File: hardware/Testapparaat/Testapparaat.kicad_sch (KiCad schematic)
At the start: 6 parts

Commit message: -enh Made the schematic for the main unit almost complete :)
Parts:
- added J7: Emergency Stop Button, symbol Connector:Mini-DIN-3
- added R14, R15, R16, R17, R18, R19, R? (x2): 10k, symbol Device:R
- added R20: 1k, symbol Device:R
- added SW3: Menu, symbol Switch:SW_Push
- added SW4: Go Back, symbol Switch:SW_Push
- added SW5: RotaryEncoder_Switch, symbol Device:RotaryEncoder_Switch
- added SW6: START, symbol Switch:SW_Push
- added SW7: STOP, symbol Switch:SW_Push
- added U4: 74AUC1G74, symbol 74xGxx:74AUC1G74
- added U5: TCA9534 (IO Expander), symbol Interface_Expansion:TCA9534
- U1: renamed from U?; value 74HC595 -> 74HC595 (SIPO Shift register)
- gave numbers to parts that had none: 5
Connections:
- net OE is gone; now on net GND: U1.13 (~{OE})
- net +3.3V: now also R14.1, R15.1, R16.1, R17.1, R18.1, R19.1, R20.1, SW5.C, U4.7 (~{PRE}), U4.8 (VCC), U5.16 (VDD)
- net GND: now also J7.2, R?.2, R?.2, SW3.2, SW4.2, SW5.S2, SW6.2, SW7.2, U4.4 (GND), U4.6 (~{CLR}), U5.1 (A0), U5.2 (A1), U5.3 (A2), U5.8 (GND)
- net I2C_SCL: now also U5.14 (SCL)
- net I2C_SDA: now also U5.15 (SDA)
- net STATUS_MOD_1: now also U1.5 (QF); no longer U1.7 (QH)
- net STATUS_MOD_2: now also U1.4 (QE); no longer U1.6 (QG)
- net TTL1_MOD_2: now also U1.2 (QC); no longer U1.3 (QD)
- net TTL2_MOD_2: now also U1.3 (QD); no longer U1.4 (QE)
- net TTL3_MOD_1: now also U5.4 (P0); no longer U1.2 (QC)
- net TTL3_MOD_2: now also U5.5 (P1); no longer U1.5 (QF)
- net SRCLR: no longer names the net of U1.10 (~{SRCLR})
- net SRCLR: now also R20.2
- new net BACK_BTN: R15.2, SW4.1, U5.10 (P5)
- new net Display_DC: U1.7 (QH)
- new net Display_RST: U1.6 (QG)
- new net EMERGENCY_STOP_BTN: J7.3, R19.2
- new net ENCODER_BTN: R16.2, SW5.S1, U5.11 (P6)
- new net IO_EXP_INT: U5.13 (~{INT})
- new net MENU_BTN: R14.2, SW3.1, U5.9 (P4)
- new net Rotary_B: R?.1, SW5.B, U4.2 (D)
- new net Rotary_CLK: R?.1, SW5.A, U4.1 (C)
- new net Rotary_DT: U4.5 (Q)
- new net START_BTN: R18.2, SW6.1, U5.6 (P2)
- new net STOP_BTN: R17.2, SW7.1, U5.7 (P3)
- no-connect marks 26 -> 28
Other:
- sheet Power Supply ports: added 5V_OUT, BATT_OUT+, BATT_OUT-; removed none
- note added: "Emergency stop using hardware (logic) is better"
- note added: "GPIO Expanders / Shift registers"
- note added: "MCU, Display, IO, SD"
- note added: "Module Ports"
- note added: "Power Supply"
- note removed: "MCU & Display"
- moved on the sheet: J2, J3, U1

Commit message: -enh Noodstop is now hardware controlled
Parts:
- added Q? (x3): IRF540N, Package_TO_SOT_THT:TO-220-3_Vertical, symbol Transistor_FET:IRF540N
- added R?: 1k, symbol Device:R
- added U? (x2): 74HC14, symbol 74xx:74HC14
- gave numbers to parts that had none: 2
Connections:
- net +3.3V: now also Q?.2 (D), U?.14 (VCC); no longer J2.5 (Pin_5), J3.5 (Pin_5)
- net +5V: now also Q?.2 (D); no longer J2.8 (Pin_8), J3.8 (Pin_8)
- net +BATT: now also Q?.2 (D); no longer J2.4 (Pin_4), J3.4 (Pin_4)
- net EMERGENCY_STOP_BTN: now also U?.1
- net GND: now also R?.2, U?.7 (GND)
- net MOD_PSU_EN: now reaches U5.12 (P7)
- net MOD_PSU_EN: now also Q?.1 (G), Q?.1 (G), Q?.1 (G), R?.1, U?.2
- new net +3.3VP: J2.5 (Pin_5), J3.5 (Pin_5), Q?.3 (S)
- new net +5VP: J2.8 (Pin_8), J3.8 (Pin_8), Q?.3 (S)
- new net +VSW: J2.4 (Pin_4), J3.4 (Pin_4), Q?.3 (S)
- no-connect marks 28 -> 27

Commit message: -enh made some changes to schematic and assigned fp
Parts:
- removed Q? (x3): IRF540N, Package_TO_SOT_THT:TO-220-3_Vertical, symbol Transistor_FET:IRF540N
- removed R?: 1k, symbol Device:R
- added C14, C15, C16, C17, C18, C19, C20: 1u, Capacitor_SMD:C_0603_1608Metric_Pad1.08x0.95mm_HandSolder, symbol Device:C
- added D1, D2, D3, D4, D5, D6, D7: 1N4448, Diode_THT:D_DO-35_SOD27_P7.62mm_Horizontal, symbol Diode:1N4448
- added Q3: BC817, Package_TO_SOT_SMD:SOT-23, symbol Transistor_BJT:BC817
- added Q4, Q5, Q6: IRF9540N, Package_TO_SOT_THT:TO-220-3_Vertical, symbol Transistor_FET:IRF9540N
- added R23, R24, R25, R26, R27, R28, R29: 10k, Resistor_SMD:R_0603_1608Metric_Pad0.98x0.95mm_HandSolder, symbol Device:R
- added R30: 1k, Resistor_SMD:R_0603_1608Metric_Pad0.98x0.95mm_HandSolder, symbol Device:R
- added R31, R32: 100k, Resistor_SMD:R_0603_1608Metric_Pad0.98x0.95mm_HandSolder, symbol Device:R
- added unit 3 of U6
- added unit 2 of U6
- added unit 4 of U6
- added unit 6 of U6
- added unit 5 of U6
- J1: footprint (none) -> Connector_Card:microSD_HC_Hirose_DM3BT-DSF-PEJS
- J2, J3: footprint (none) -> Connector_PinHeader_2.54mm:PinHeader_2x12_P2.54mm_Horizontal
- J7: footprint (none) -> Connector_PinHeader_2.54mm:PinHeader_1x03_P2.54mm_Horizontal
- R1, R14, R15, R16, R17, R18, R19, R2, R20, R21, R22: footprint (none) -> Resistor_SMD:R_0603_1608Metric_Pad0.98x0.95mm_HandSolder
- SW3, SW6, SW7: footprint (none) -> Button_Switch_SMD:SW_SPST_B3S-1000
- SW4: value Go Back -> Back; footprint (none) -> Button_Switch_SMD:SW_SPST_B3S-1000
- SW5: footprint (none) -> Rotary_Encoder:RotaryEncoder_Alps_EC11E-Switch_Vertical_H20mm_CircularMountingHoles
- U1: footprint (none) -> Package_SO:SO-16_3.9x9.9mm_P1.27mm
- U4: footprint (none) -> Package_SO:VSSOP-8_2.3x2mm_P0.5mm
- U5: footprint (none) -> Package_SO:TSSOP-16_4.4x5mm_P0.65mm
- U6: renamed from U?; footprint (none) -> Package_SO:SO-14_3.9x8.65mm_P1.27mm
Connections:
- net +3.3V: now also R21.2, SW3.2, SW4.2, U4.6 (~{CLR}), Q4.3 (S), R26.2; no longer R14.1, R15.1, SW5.C
- net +3.3VP: now also Q4.2 (D)
- net +5V: now also Q5.3 (S)
- net +5VP: now also Q5.2 (D)
- net +BATT: now also Q6.3 (S), R31.1
- net +VSW: now also Q6.2 (D)
- net BACK_BTN: now also C15.1, D2.1 (K), R23.2; no longer R15.2, SW4.1
- net ENCODER_BTN: now also U6.12; no longer R16.2, SW5.S1
- net GND: now also R14.2, R15.2, SW5.C, C14.2, C15.2, C16.2, C17.2, C18.2, C19.2, C20.2, Q3.2 (E), R32.2; no longer R21.2, R22.2, SW3.2, SW4.2, U4.6 (~{CLR})
- net MENU_BTN: now also R22.2, C14.1, D1.1 (K); no longer R14.2, SW3.1
- net MOD_PSU_EN: now also R30.1
- net Rotary_B: now also U6.4; no longer R22.1, SW5.B
- net Rotary_CLK: now also U6.6; no longer R21.1, SW5.A
- net START_BTN: now also U6.8; no longer R18.2, SW6.1
- net STOP_BTN: now also U6.10; no longer R17.2, SW7.1
- new net: C16.1, D3.1 (K), R24.2, U6.5
- new net: D2.2 (A), R15.1, R23.1, SW4.1
- new net: C19.1, D7.1 (K), R29.2, U6.11
- new net: D4.2 (A), R25.1, R26.1, SW5.B
- new net: R21.1, SW5.A
- new net: D1.2 (A), R14.1, R22.1, SW3.1
- new net: C18.1, D6.1 (K), R28.2, U6.9
- new net: D6.2 (A), R18.2, R28.1, SW6.1
- new net: Q3.1 (B), R30.2, R32.1
- new net: C17.1, D4.1 (K), R25.2, U6.3
- new net: D7.2 (A), R17.2, R29.1, SW7.1
- new net: Q3.3 (C), Q4.1 (G), Q5.1 (G), Q6.1 (G), R31.2
- new net: D3.2 (A), R24.1
- new net: C20.1, D5.1 (K), R27.1, U6.13
- new net: D5.2 (A), R16.2, R27.2, SW5.S1
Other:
- note removed: "Emergency stop using hardware (logic) is better"
- moved on the sheet: R14, R15, R16, R17, R18, R20, R21, SW5, SW6, SW7, U1, U4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

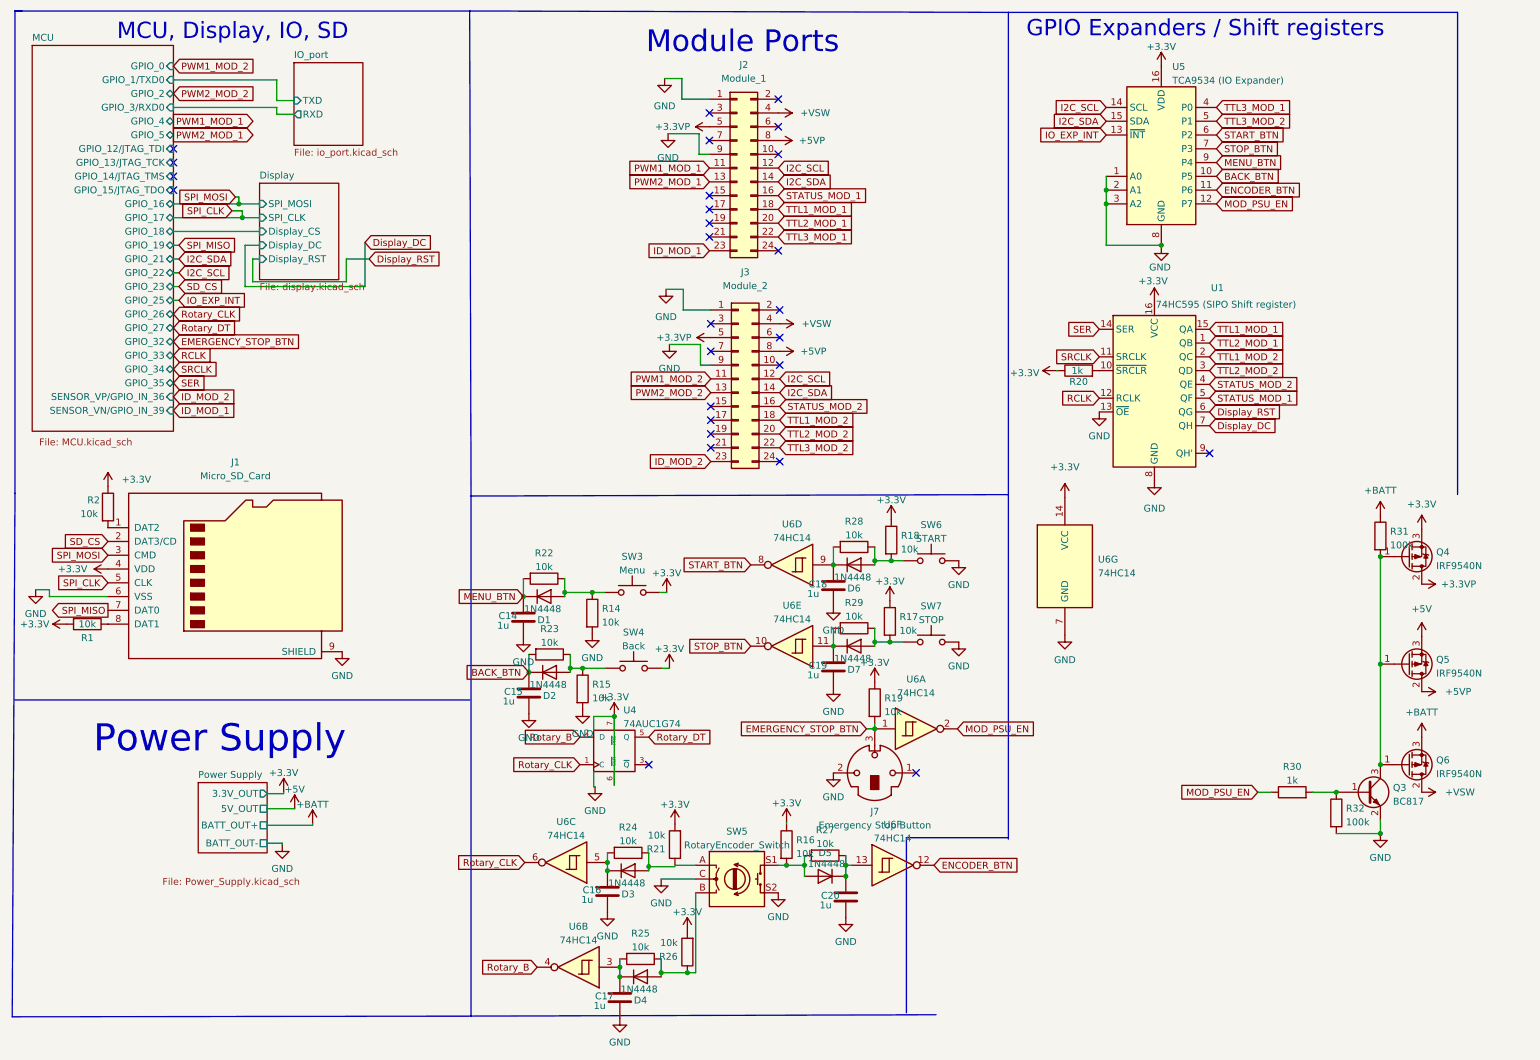
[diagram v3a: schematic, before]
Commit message: -enh add seperate schematic and pcb for io ports/slots
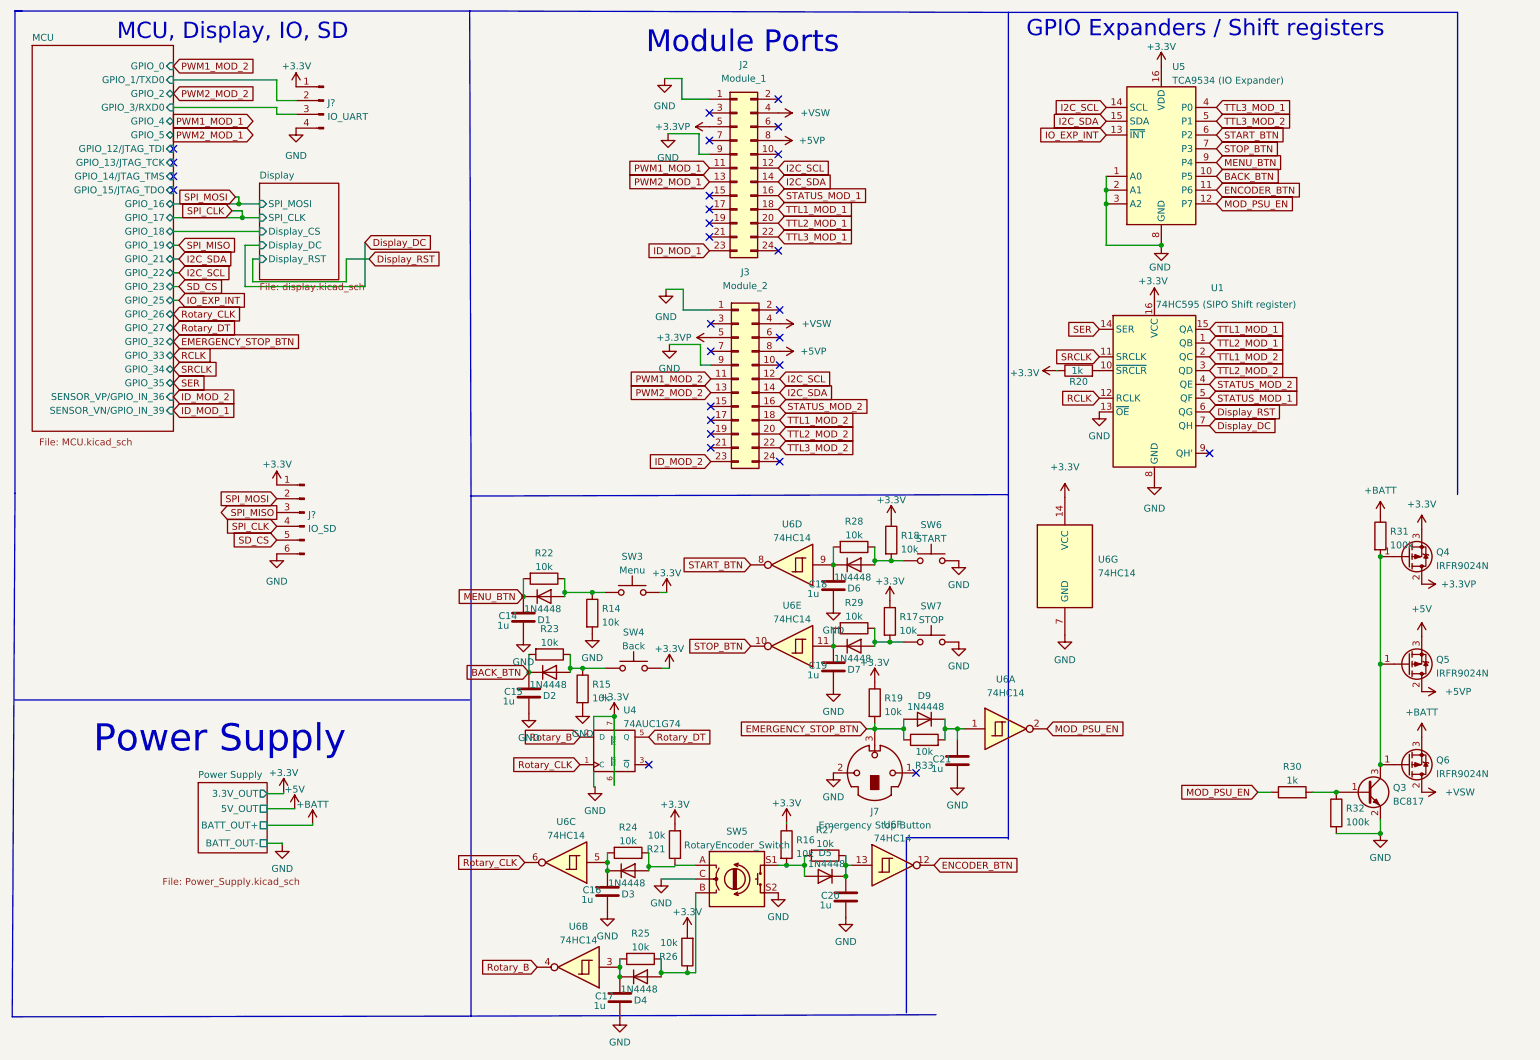
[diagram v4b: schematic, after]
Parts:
- removed J1: Micro_SD_Card, Connector_Card:microSD_HC_Hirose_DM3BT-DSF-PEJS, symbol Connector:Micro_SD_Card
- removed R1, R2: 10k, Resistor_SMD:R_0603_1608Metric_Pad0.98x0.95mm_HandSolder, symbol Device:R
- added C21: 1u, Capacitor_SMD:C_0603_1608Metric_Pad1.08x0.95mm_HandSolder, symbol Device:C
- added D9: 1N4448, Diode_THT:D_DO-35_SOD27_P7.62mm_Horizontal, symbol Diode:1N4448
- added J?: IO_UART, symbol Connector:Conn_01x04_Male
- added J?: IO_SD, symbol Connector:Conn_01x06_Male
- added R33: 10k, Resistor_SMD:R_0603_1608Metric_Pad0.98x0.95mm_HandSolder, symbol Device:R
- Q4, Q5, Q6: value IRF9540N -> IRFR9024N; footprint Package_TO_SOT_THT:TO-220-3_Vertical -> Package_TO_SOT_SMD:TO-252-3_TabPin2
- U1: footprint Package_SO:SO-16_3.9x9.9mm_P1.27mm -> 74HC595D-Q100,118:74HC595DQ100118
- U5: footprint Package_SO:TSSOP-16_4.4x5mm_P0.65mm -> TCA9534:SOP65P640X120-16N
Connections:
- net +3.3V: now also J?.1 (Pin_1), J?.1 (Pin_1)
- net EMERGENCY_STOP_BTN: now also D9.2 (A), R33.1; no longer U6.1
- net GND: now also C21.2, J?.4 (Pin_4), J?.6 (Pin_6)
- net SD_CS: now also J?.5 (Pin_5)
- net SPI_CLK: now also J?.4 (Pin_4)
- net SPI_MISO: now also J?.3 (Pin_3)
- net SPI_MOSI: now also J?.2 (Pin_2)
- new net: C21.1, D9.1 (K), R33.2, U6.1
- new net MCU/GPIO_1/TXD0: J?.2 (Pin_2)
- new net MCU/GPIO_3/RXD0: J?.3 (Pin_3)
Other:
- removed sheet IO_port
- moved on the sheet: U6A

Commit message: -add BOM
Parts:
- removed C14, C15, C16, C17, C18, C19, C20: 1u, Capacitor_SMD:C_0603_1608Metric_Pad1.08x0.95mm_HandSolder, symbol Device:C
- removed D1, D2, D3, D4, D5, D6, D7: 1N4448, Diode_THT:D_DO-35_SOD27_P7.62mm_Horizontal, symbol Diode:1N4448
- removed R14, R15, R16, R17, R18, R21, R22, R23, R24, R25, R26, R27, R28, R29: 10k, Resistor_SMD:R_0603_1608Metric_Pad0.98x0.95mm_HandSolder, symbol Device:R
- removed SW3: Menu, Button_Switch_SMD:SW_SPST_B3S-1000, symbol Switch:SW_Push
- removed SW4: Back, Button_Switch_SMD:SW_SPST_B3S-1000, symbol Switch:SW_Push
- removed SW5: RotaryEncoder_Switch, Rotary_Encoder:RotaryEncoder_Alps_EC11E-Switch_Vertical_H20mm_CircularMountingHoles, symbol Device:RotaryEncoder_Switch
- removed SW6: START, Button_Switch_SMD:SW_SPST_B3S-1000, symbol Switch:SW_Push
- removed SW7: STOP, Button_Switch_SMD:SW_SPST_B3S-1000, symbol Switch:SW_Push
- removed U4: 74AUC1G74, Package_SO:VSSOP-8_2.3x2mm_P0.5mm, symbol 74xGxx:74AUC1G74
- removed unit 3 of U6
- removed unit 2 of U6
- removed unit 4 of U6
- removed unit 6 of U6
- removed unit 7 of U6
- removed unit 5 of U6
- added C14, C15, C16, C17: 100n, Capacitor_SMD:C_0603_1608Metric_Pad1.08x0.95mm_HandSolder, symbol Device:C_Small
- added J14: GPIO_OUTPUT, Connector_PinHeader_2.54mm:PinHeader_2x04_P2.54mm_Vertical_SMD, symbol Connector:Conn_01x08_Male
- added R1: 1k, Resistor_SMD:R_0603_1608Metric_Pad0.98x0.95mm_HandSolder, symbol Device:R
- added U3: 74AHC1G02, 74AHC1G02:SOTFL50P160X60-5N, symbol 74xGxx:74AHC1G02
- added U4: 74HC595 (SIPO Shift register), 74HC595D-Q100,118:74HC595DQ100118, symbol 74xx:74HC595
- added U7: TCA9534 (IO Expander), TCA9534:SOP65P640X120-16N, symbol Interface_Expansion:TCA9534
- J1: renamed from J?; footprint (none) -> Connector_PinHeader_2.54mm:PinHeader_1x06_P2.54mm_Horizontal
- J6: renamed from J?; footprint (none) -> Connector_PinHeader_2.54mm:PinHeader_1x04_P2.54mm_Horizontal
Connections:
- net START_BTN is gone; now on net EMERGENCY_STOP_BTN: U5.6 (P2)
- net +3.3V: now also C21.2, J1.6 (Pin_6), J2.1 (Pin_1), J2.9 (Pin_9), J3.1 (Pin_1), J3.9 (Pin_9), J6.4 (Pin_4), J7.1, Q3.2 (E), R32.2, U1.8 (GND), U5.1 (A0), U5.2 (A1), U5.3 (A2), U5.8 (GND), C14.1, C14.2, C15.1, C15.2, C16.1, C16.2, C17.1, C17.2, R1.1, U3.3 (GND), U3.5 (VCC), U4.16 (VCC), U4.8 (GND), U7.1 (A0), U7.16 (VDD), U7.2 (A1), U7.3 (A2), U7.8 (GND)
- net I2C_SCL: now also U7.14 (SCL)
- net I2C_SDA: now also U7.15 (SDA)
- net IO_EXP_INT: now also U3.4; no longer U5.13 (~{INT})
- net MOD_PSU_EN: no longer U5.12 (P7)
- net RCLK: now also U4.12 (RCLK)
- net SPI_CLK: now also J1.3 (Pin_3); no longer J1.4 (Pin_4)
- net SPI_MISO: now also J1.2 (Pin_2); no longer J1.3 (Pin_3)
- net SPI_MOSI: now also J1.4 (Pin_4); no longer J1.2 (Pin_2)
- net SRCLK: now also U4.11 (SRCLK)
- net at U1.9 (QH'): now also U4.14 (SER)
- net BACK_BTN renamed BTN_2
- net ENCODER_BTN renamed BTN_3
- removed net GND: C21.2, J1.6 (Pin_6), J2.1 (Pin_1), J2.9 (Pin_9), J3.1 (Pin_1), J3.9 (Pin_9), J6.4 (Pin_4), J7.2, Q3.2 (E), R32.2, U1.13 (~{OE}), U1.8 (GND), U5.1 (A0), U5.2 (A1), U5.3 (A2), U5.8 (GND)
- net MENU_BTN renamed BTN_1
- net STOP_BTN renamed Rotary_BTN
- new net: R1.2, U4.10 (~{SRCLR})
- new net: U3.2, U7.13 (~{INT})
- new net: U3.1, U5.13 (~{INT})
- new net BTN_10: U7.10 (P5)
- new net BTN_4: U5.12 (P7)
- new net BTN_5: U7.4 (P0)
- new net BTN_6: U7.5 (P1)
- new net BTN_7: U7.6 (P2)
- new net BTN_8: U7.7 (P3)
- new net BTN_9: U7.9 (P4)
- new net GPIO_INPUT_1: U7.11 (P6)
- new net GPIO_INPUT_2: U7.12 (P7)
- new net GPIO_OUTPUT_1: J14.1 (Pin_1), U4.15 (QA)
- new net GPIO_OUTPUT_2: J14.2 (Pin_2), U4.1 (QB)
- new net GPIO_OUTPUT_3: J14.3 (Pin_3), U4.2 (QC)
- new net GPIO_OUTPUT_4: J14.4 (Pin_4), U4.3 (QD)
- new net GPIO_OUTPUT_5: J14.5 (Pin_5), U4.4 (QE)
- new net GPIO_OUTPUT_6: J14.6 (Pin_6), U4.5 (QF)
- new net GPIO_OUTPUT_7: J14.7 (Pin_7), U4.6 (QG)
- new net GPIO_OUTPUT_8: J14.8 (Pin_8), U4.7 (QH)
- new net OE: U1.13 (~{OE}), U4.13 (~{OE})
- no-connect marks 27 -> 26
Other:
- added sheet button_inputs (button_inputs.kicad_sch)
- moved on the sheet: C21, D9, J7, Q3, Q4, Q5, Q6, R19, R20, R30, R31, R32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
